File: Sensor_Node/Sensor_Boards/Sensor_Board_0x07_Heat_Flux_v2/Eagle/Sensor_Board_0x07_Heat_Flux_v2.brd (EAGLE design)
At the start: 55 x 35 mm, 14 parts, among them J1 M04_SMD_90, J4 ARDUINO_ISP, U2 ATMEGA328P_TQFP, Y1 8MHZ

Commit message: Work on heat flux sensor continued
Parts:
- removed R1: 10k, SparkFun-Passives:0805
- removed S3: JS202011SCQN, myownthings:JS202011SCQN
- added C4, C5, C6, C8: 100n, eagle-ltspice:C0805
- added C7: 1u, eagle-ltspice:C0805
- added D1: LEDXLAMP_BAV99, Sensor_Board_0x07_Heat_Flux:LEDXLAMP_SOT23
- added IC1: HEATFLOW_MCP3911A0-E/SS, Sensor_Board_0x07_Heat_Flux:HEATFLOW_SSOP20
- added IC2: 40XX_4066D, Sensor_Board_0x07_Heat_Flux:40XX_SO14
- added L1: HEATFLOW2_74279220601, Sensor_Board_0x07_Heat_Flux:HEATFLOW2_0805
- added PAD1, PAD2: WIREPADSMD1,27-254, wirepad:SMD1,27-2,54
- added R4, R5: 10k, SparkFun-Passives:0805
- added R6: 0, Sensor_Board_0x07_Heat_Flux:RESISTOR_M0805
- moved S1 9.69 mm to (28.9, 24.8), turned to 90 degrees
- moved R2 3.82 mm to (32.7, 10.8), turned to 0 degrees
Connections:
- removed net DBG_ENABLE: R1.2, U2.26
- removed net GND: C2.2, C3.2, J1.4, J4.P$5, LED1.C, S1.1, S1.2, S3.3, SV1.1, SV1.2, U2.21, U2.3, U2.5, Y1.2
- removed net N$3: R1.1, S3.2
- removed net VCC: C2.1, J1.1, J4.P$6, R2.2, S3.1, SV1.3, U2.18, U2.4, U2.6
- new net AGND: C4.1, C5.2, C7.2, D1.1, D1.2, IC1.10, IC1.5, IC1.6, IC1.7, IC1.8, IC2.1, PAD2.1, R6.2
- new net AVCC: C5.1, IC1.3, L1.2
- new net DGND: C2.2, C3.2, C6.2, C8.2, IC1.11, IC2.11, IC2.12, IC2.6, IC2.7, IC2.8, J1.4, J4.P$5, LED1.C, R6.1, S1.1, S1.2, SV1.1, SV1.2, U2.21, U2.3, U2.5, Y1.2
- new net DVCC: C2.1, C6.1, C8.1, IC1.2, IC2.14, J1.1, J4.P$6, L1.1, R2.2, R4.2, R5.2, SV1.3, U2.18, U2.4, U2.6
- new net INPUT_EN: IC2.5, U2.23
- new net INPUT_SHORT: IC2.13, U2.24
- new net MCP_CLK: IC1.15, U2.13
- new net MCP_CS: IC1.17, R4.1, U2.12
- new net MCP_DATA_RDY: IC1.14, U2.1
- new net MCP_RESET: IC1.1, R5.1, U2.25
- new net N$4: C4.2, IC1.9
- new net N$5: IC1.4, IC2.2, IC2.3
- new net N$6: C7.1, D1.3, IC2.4, PAD1.1
- net MISO: now also IC1.19
- net MOSI: now also IC1.20
- net SCK: now also IC1.18
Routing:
- net VCC: track 57.7 -> 0.00 mm, vias 2 -> 0
- net GND: track 57.0 -> 0.00 mm, vias 6 -> 0
- net DGND: track 0.00 -> 30.3 mm, vias 0 -> 7
- net N$3: track 14.8 -> 0.00 mm
- net DBG_ENABLE: track 14.5 -> 0.00 mm, vias 2 -> 0
- net RESET: track 45.8 -> 39.2 mm
- net DVCC: track 0.00 -> 3.62 mm, vias 0 -> 2
- added copper zone on layer 16, net DGND
- added copper zone on layer 1, net DVCC
- removed copper zone on layer 16, net GND

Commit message: Worked on heat flux board
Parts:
- added C10: 100n, eagle-ltspice:C0805
- added C9: 10n, eagle-ltspice:C0805
- added FB1, FB2: (no value), Adafruit_MAX31855 v2:MICROBUILDER__0805MP
- added IC4: ADAFRUIT_MAX31855, Adafruit_MAX31855 v2:ADAFRUIT_SO08
- added PAD10, PAD3, PAD4, PAD5, PAD6, PAD7, PAD8, PAD9: WIREPADSMD1,27-254, wirepad:SMD1,27-2,54
- added R1, R7, R8: 10k, SparkFun-Passives:0805
- moved IC1 38.5 mm to (33.0, 5.71), turned to 270 degrees
- moved R2 13.7 mm to (35.9, 24.1)
- moved S1 10.6 mm to (27.0, 14.3)
- moved C1 1.27 mm to (36.8, 26.7)
- moved C2 0.95 mm to (36.8, 29.5)
- moved C3 0.63 mm to (36.8, 32.4)
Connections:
- removed net SCL: U2.28
- removed net SDA: U2.27
- new net DS18B20_DATA_1: PAD4.1, R1.1, U2.26
- new net DS18B20_DATA_2: PAD7.1, R7.1, U2.25
- new net MAX_CS: IC4.6, R8.1, U2.24
- new net N$3: FB1.1, PAD9.1
- new net N$7: FB2.1, PAD10.1
- new net N$8: C9.2, FB2.2, IC4.2
- new net N$9: C9.1, FB1.2, IC4.3
- net DGND: now also C10.2, IC4.1, PAD5.1, PAD8.1
- net DVCC: now also C10.1, IC4.4, PAD3.1, PAD6.1, R1.2, R7.2, R8.2
- net INPUT_SHORT: now also U2.2; no longer U2.24
- net MCP_CS: now also U2.9; no longer U2.12
- net MCP_RESET: now also U2.12; no longer U2.25
- net MISO: now also IC4.7
- net SCK: now also IC4.5
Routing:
- net MISO: track 13.6 -> 51.0 mm, vias 2 -> 5
- net DS18B20_DATA_1: track 0.00 -> 35.5 mm, vias 0 -> 2
- net SCK: track 15.1 -> 48.2 mm, vias 2 -> 5
- net DS18B20_DATA_2: track 0.00 -> 27.4 mm, vias 0 -> 2
- net MCP_CLK: track 0.00 -> 16.9 mm, vias 0 -> 2
- net MAX_CS: track 0.00 -> 14.0 mm, vias 0 -> 2
- net MCP_CS: track 0.00 -> 13.9 mm, vias 0 -> 2
- net DVCC: track 3.62 -> 17.1 mm, vias 2 -> 4
- net MOSI: track 18.4 -> 31.2 mm, vias 2 -> 4
- net N$9: track 0.00 -> 10.9 mm
- net N$8: track 0.00 -> 10.1 mm
- net MCP_RESET: track 0.00 -> 9.24 mm, vias 0 -> 2
- net N$7: track 0.00 -> 7.13 mm
- net DGND: track 30.3 -> 34.9 mm, vias 7 -> 11
- net N$3: track 0.00 -> 3.55 mm
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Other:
- board text removed: "DEBUG"

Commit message: Continued on Heat Flux v2
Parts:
- moved S1 1.27 mm to (27.0, 13.0)
- moved R8 1.00 mm to (30.2, 23.8), turned to 0 degrees
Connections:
- net MCP_CS: now also U2.12; no longer U2.9
- net MCP_RESET: now also U2.9; no longer U2.12
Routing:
- net INPUT_EN: track 0.00 -> 14.0 mm, vias 0 -> 2
- net MCP_RESET: track 9.24 -> 22.7 mm
- net MCP_DATA_RDY: track 0.00 -> 11.9 mm, vias 0 -> 2
- net DVCC: track 17.1 -> 24.8 mm, vias 4 -> 8
- net INPUT_SHORT: track 0.00 -> 7.03 mm
- net SCK: track 48.2 -> 52.2 mm
- net MISO: track 51.0 -> 53.7 mm
- net MAX_CS: track 14.0 -> 16.6 mm
- net MOSI: track 31.2 -> 33.4 mm
- net DGND: track 34.9 -> 37.2 mm, vias 11 -> 12
- net MCP_CS: track 13.9 -> 15.8 mm
- net RESET: track 38.3 -> 39.6 mm
- net MCU_RXI: track 17.5 -> 16.5 mm
- net FTDI_TXO: track 20.1 -> 20.9 mm

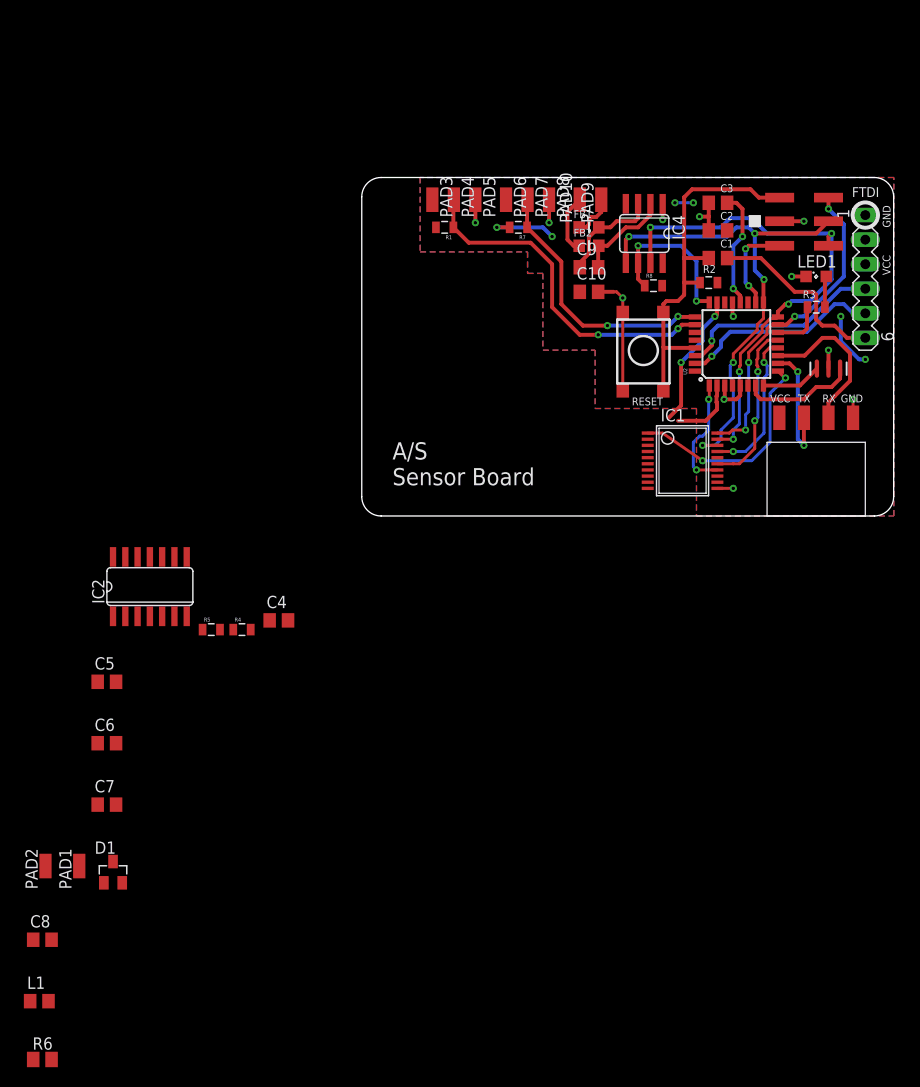
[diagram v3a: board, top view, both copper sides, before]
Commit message: Finished routing of heat flux v2
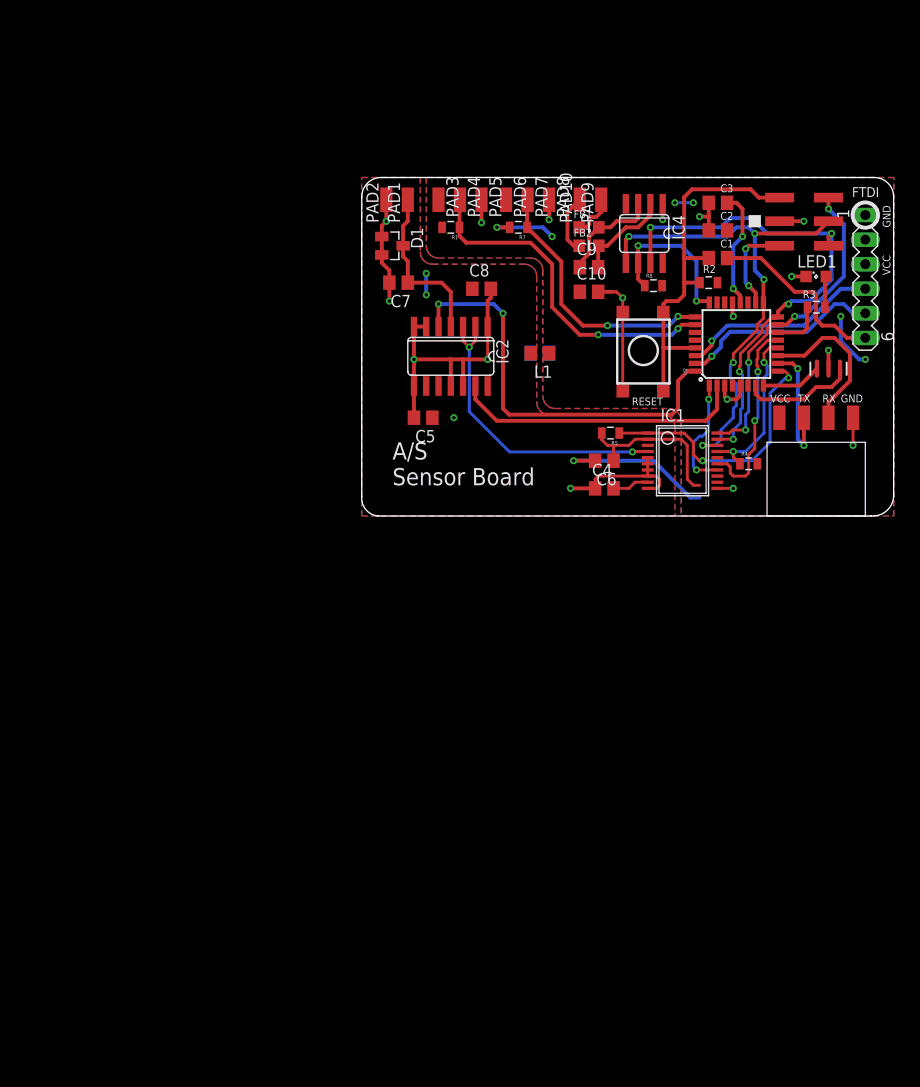
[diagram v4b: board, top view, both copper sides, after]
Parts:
- moved R6 89.3 mm to (18.4, 16.8), flipped to the bottom
- moved L1 84.7 mm to (18.4, 16.8), turned to 180 degrees
- moved C8 81.2 mm to (12.4, 23.5)
- moved PAD2 77.4 mm to (2.54, 32.7)
- moved PAD1 76.8 mm to (4.76, 32.7)
- moved D1 70.9 mm to (3.17, 27.9), turned to 270 degrees
- moved C7 61.8 mm to (3.81, 24.1), turned to 180 degrees
- moved C6 59.2 mm to (25.1, 5.71), turned to 180 degrees
- moved R4 55.1 mm to (40.0, 5.40)
- moved R5 46.0 mm to (25.7, 8.57), turned to 180 degrees
- moved C5 42.6 mm to (6.35, 10.2), turned to 180 degrees
- moved IC2 39.2 mm to (9.21, 16.5), turned to 180 degrees
- moved C4 36.3 mm to (25.1, 2.86)
- moved PAD3 0.63 mm to (7.94, 32.7)
- moved PAD4 0.63 mm to (10.2, 32.7)
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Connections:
- net AGND: now also C8.2, IC2.11, IC2.12, IC2.6, IC2.7, IC2.8
- net AVCC: now also C8.1, IC2.14
- net DGND: no longer C8.2, IC2.11, IC2.12, IC2.6, IC2.7, IC2.8
- net DVCC: no longer C8.1, IC2.14
- net INPUT_EN: now also U2.32; no longer U2.23
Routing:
- net AGND: track 0.00 -> 56.8 mm, vias 0 -> 5
- net N$5: track 0.00 -> 31.6 mm, vias 0 -> 2
- net INPUT_EN: track 14.0 -> 42.9 mm
- net INPUT_SHORT: track 7.03 -> 30.2 mm
- net DGND: track 37.2 -> 55.0 mm, vias 12 -> 13
- net N$6: track 0.00 -> 17.4 mm
- net DVCC: track 24.8 -> 41.8 mm
- net MCP_RESET: track 22.7 -> 27.6 mm
- net N$4: track 0.00 -> 3.80 mm
- net MCP_CLK: track 17.4 -> 19.9 mm
- net AVCC: track 0.00 -> 2.22 mm, vias 0 -> 2
- net MCP_CS: track 15.8 -> 17.3 mm
- net N$3: track 3.55 -> 4.50 mm
- net FTDI_RXI: track 21.6 -> 21.1 mm
- added copper zone on layer 16, net AGND
- added copper zone on layer 1, net AVCC
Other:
- outline, holes or cut-outs redrawn

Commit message: Weiterarbeit Heat Flux
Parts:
- moved L1 0.64 mm to (18.4, 16.2)
- moved R6 0.64 mm to (18.4, 16.2)
- renumbered LED1 to LED
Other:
- board text added: "ADC"
- board text added: "MAX"

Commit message: Finished sensorboard heat flux v2
- added BOM
- added PDF's
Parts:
- IC1: value HEATFLOW_MCP3911A0-E/SS -> MCP3911
- IC4: value ADAFRUIT_MAX31855 -> MAX31855
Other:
- board text added: "A/S Sensor Board Heat Flux"
- board text added: "DATA"
- board text added: "DS18B20"
- board text added: "IN1"
- board text added: "IN2"
- board text added: "MAX31855"
- board text added: "MCP3911"
- board text added: "T-COUPLE"
- board text added: "UIN"
- board text added: "uV Input"
- board text removed: "A/S Sensor Board"
- board text removed: "ADC"
- board text removed: "MAX"
